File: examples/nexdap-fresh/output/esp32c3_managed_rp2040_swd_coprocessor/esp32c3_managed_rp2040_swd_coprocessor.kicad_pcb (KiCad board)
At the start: 2 copper layers, 63 parts, among them J1 USB-C-16P

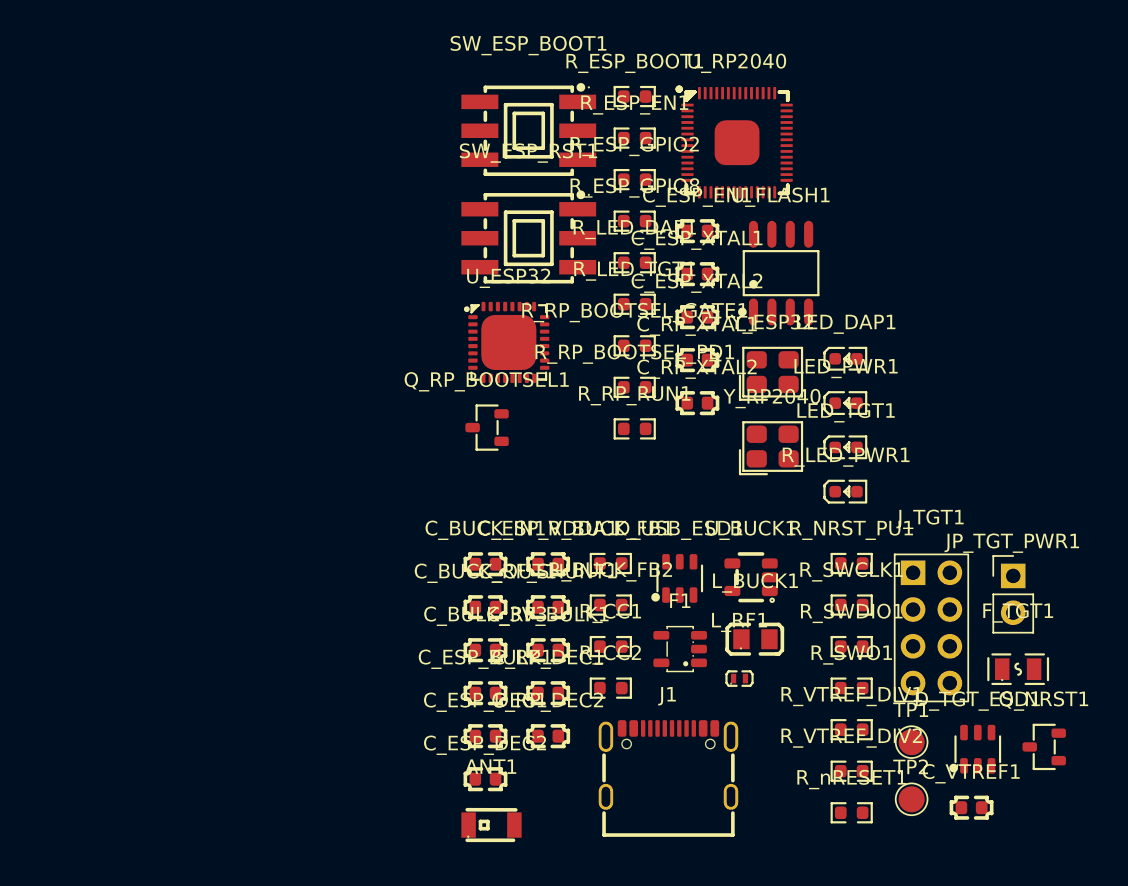
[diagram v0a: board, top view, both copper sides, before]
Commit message: Update NexDAP example outputs and fix KiCad mapping logic / 更新 NexDAP 示例输出并修正 KiCad 映射逻辑
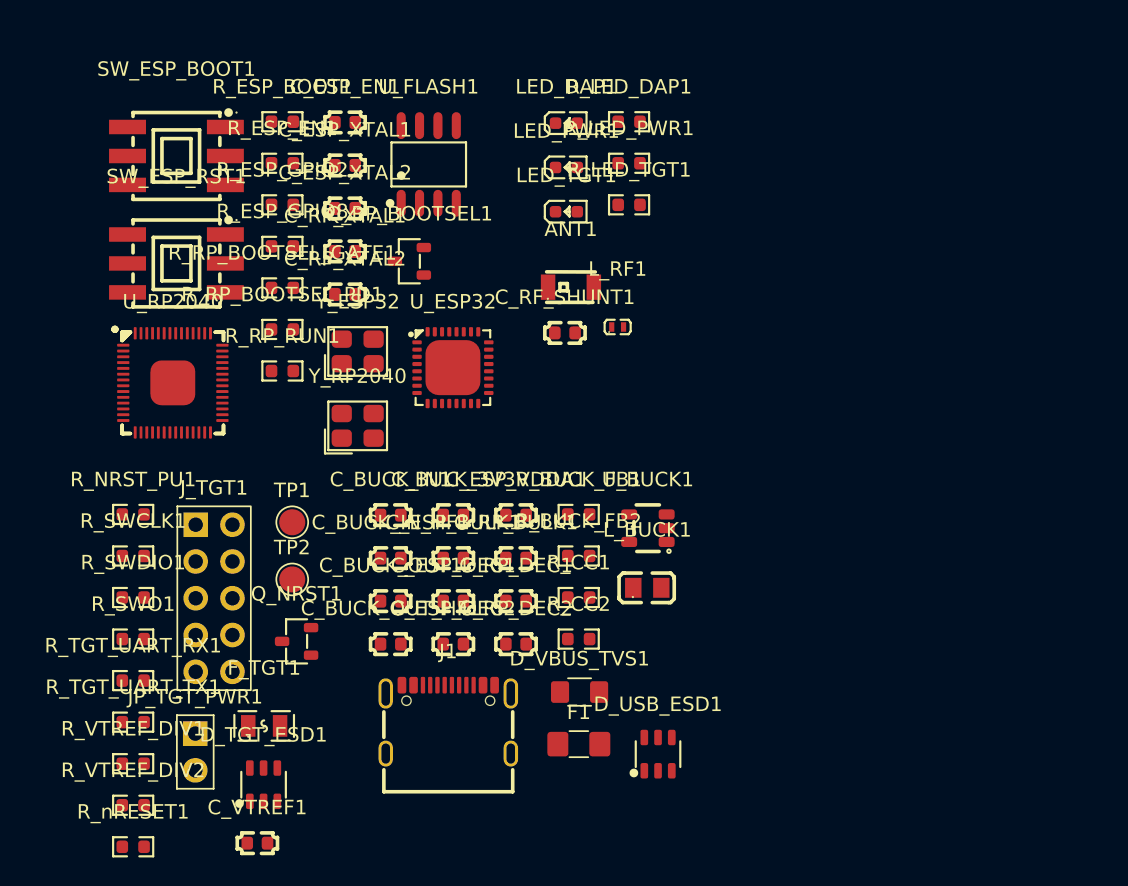
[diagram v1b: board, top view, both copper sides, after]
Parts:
- added C_BUCK_IN_HF1: 100nF, JLC-MCP:C0603, F.Cu at (132.5, 108.0)
- added C_BUCK_OUT_HF1: 100nF, JLC-MCP:C0603, F.Cu at (132.5, 114.0)
- added D_VBUS_TVS1: SMF5.0A, JLC-MCP:SMF5.0A, F.Cu at (145.6, 117.3)
- added R_TGT_UART_RX1: 22R, JLC-MCP:R0603, F.Cu at (114.8, 116.5)
- added R_TGT_UART_TX1: 22R, JLC-MCP:R0603, F.Cu at (114.8, 119.3)
- C_BUCK_IN1, C_BULK_3V3: value 10uF -> 22uF
- F1: value MNCP380HSN05AAT1G -> SMD1206-050-33; footprint JLC-MCP:SOT-23-5_L3.0-W1.7-P0.95-LS2.8-BR -> JLC-MCP:SMD1206-050-33
- JP_TGT_PWR1: footprint Connector_PinHeader_2.54mm:PinHeader_1x02_P2.54mm_Vertical -> JLC-MCP:HDR-TH_2P-P2.54-V-M
- J_TGT1: value Header-2.54-2x4P -> Header-2.54-2x5P; footprint JLC-MCP:HDR-TH_8P-P2.54-V-M-2X4 -> JLC-MCP:HDR-TH_10P-P2.54-V-M-2X5
- R_BUCK_FB1: value 100k -> 453k
- R_BUCK_FB2: value 33k -> 100k
- R_LED_PWR1: footprint JLC-MCP:LED0603-RD -> JLC-MCP:R0603
- moved JP_TGT_PWR1 57.5 mm to (119.0, 120.1)
- moved F_TGT1 52.2 mm to (123.8, 119.6)
- moved Q_NRST1 52.2 mm to (126.0, 113.8)
- moved R_NRST_PU1 49.8 mm to (114.8, 105.0)
- moved R_SWCLK1 49.8 mm to (114.8, 107.9)
- moved R_SWDIO1 49.8 mm to (114.8, 110.7)
- moved R_SWO1 49.8 mm to (114.8, 113.6)
- moved R_VTREF_DIV2 49.7 mm to (114.8, 125.1)
- moved R_VTREF_DIV1 49.7 mm to (114.8, 122.2)
- moved R_nRESET1 49.7 mm to (114.8, 128.0)
- moved C_VTREF1 49.4 mm to (123.3, 127.7)
- moved D_TGT_ESD1 49.4 mm to (123.8, 123.7)
- moved J_TGT1 48.3 mm to (120.3, 110.8)
- moved TP1 45.4 mm to (125.7, 105.5)
- moved TP2 45.4 mm to (125.7, 109.5)
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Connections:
- net /01_power/ESP_RF_OUT renamed /03_rf/ESP_RF_OUT
- net /01_power/RF_ANT renamed /03_rf/RF_ANT
- net /02_mcu/LED_DAP_A renamed /05_indicator/LED_DAP_A
- net /02_mcu/LED_PWR_A renamed /05_indicator/LED_PWR_A
- net /02_mcu/LED_TGT_K renamed /05_indicator/LED_TGT_K
- net /03_target/ESP_RP_SWCLK renamed /04_target/RP_TGT_SWCLK
- net /03_target/ESP_RP_SWDIO renamed /04_target/RP_TGT_SWDIO
- net /03_target/HOST_SWO_IN renamed /04_target/TGT_SWO_IN
- net /03_target/HOST_nRESET_CTRL renamed /04_target/HOST_nRESET_CTRL
- net /03_target/TGT_SWCLK renamed /04_target/TGT_SWCLK
- net /03_target/TGT_SWDIO renamed /04_target/TGT_SWDIO
- net /03_target/TGT_SWO_OUT renamed /04_target/TGT_SWO_OUT
- net /03_target/TGT_nRESET renamed /04_target/TGT_nRESET
- net /03_target/TGT_nRESET_DRV renamed /04_target/TGT_nRESET_DRV
- net /03_target/VTREF_TARGET renamed /04_target/VTREF_ADC
- D_TGT_ESD1 pad 5: +3V3_MAIN -> /04_target/VTREF_TARGET
- F_TGT1 pad 2: +5V_SW_TGT -> +5V_TGT_FUSED
- JP_TGT_PWR1 pad 1: +5V_SW_TGT -> +5V_TGT_FUSED
- J_TGT1 pad 1: +5V_SW_TGT -> /04_target/VTREF_TARGET
- J_TGT1 pad 7: unconnected-(J_TGT1-Pad7) -> /04_target/TGT_UART_TX
- J_TGT1 pad 8: unconnected-(J_TGT1-Pad8) -> /04_target/TGT_UART_RX
- LED_DAP1 pad 1: /02_mcu/DAP_ACTIVITY -> /05_indicator/DAP_ACTIVITY
- R_LED_TGT1 pad 1: +3V3_MAIN -> +5V_SW_TGT
- R_NRST_PU1 pad 1: +3V3_MAIN -> /04_target/VTREF_TARGET
- R_VTREF_DIV1 pad 1: +3V3_MAIN -> /04_target/VTREF_TARGET
- U_BUCK1 pad 1: +3V3_MAIN -> +5V_USB_PROTECTED
- U_ESP32 pad 27: /02_mcu/ESP_TO_RP_IRQ -> /02_mcu/ESP_RP_BOOTSEL_CTRL
- U_RP2040 pad 13: /02_mcu/ESP_TO_RP_IRQ -> unconnected-(U_RP2040-GPIO10-Pad13)
- U_RP2040 pad 19: unconnected-(U_RP2040-TESTEN-Pad19) -> GND_HOST
- U_RP2040 pad 2: unconnected-(U_RP2040-GPIO0-Pad2) -> /02_mcu/RP_TGT_SWCLK
- U_RP2040 pad 3: unconnected-(U_RP2040-GPIO1-Pad3) -> /02_mcu/RP_TGT_SWDIO
- U_RP2040 pad 38: unconnected-(U_RP2040-GPIO26_ADC0-Pad38) -> /02_mcu/VTREF_ADC
- U_RP2040 pad 43: unconnected-(U_RP2040-ADC_AVDD-Pad43) -> +3V3_MAIN
- U_RP2040 pad 6: /02_mcu/HOST_SWO_IN -> unconnected-(U_RP2040-GPIO4-Pad6)
- U_RP2040 pad 7: unconnected-(U_RP2040-GPIO5-Pad7) -> /02_mcu/TGT_SWO_IN
- U_RP2040 pad 8: unconnected-(U_RP2040-GPIO6-Pad8) -> /02_mcu/RP_TGT_UART_TX
- U_RP2040 pad 9: unconnected-(U_RP2040-GPIO7-Pad9) -> /02_mcu/RP_TGT_UART_RX
